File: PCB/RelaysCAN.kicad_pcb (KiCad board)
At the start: 2 copper layers, 200 x 100 mm, 99 parts, among them J1 Screw_Terminal_01x03, J2 Screw_Terminal_01x02, J3 Conn_01x24_Male, J4 Conn_01x24_Male, J5 Conn_01x24_Male, J6 Conn_01x24_Male, J7 Conn_01x24_Male, J8 Conn_01x24_Male, K1 ALQ112, K10 ALQ112, K11 ALQ112, K12 ALQ112, K13 ALQ112, K14 ALQ112, K15 ALQ112, K16 ALQ112, K17 ALQ112, K18 ALQ112, K19 ALQ112, K2 ALQ112, K20 ALQ112, K21 ALQ112, K22 ALQ112, K23 ALQ112, K24 ALQ112, K3 ALQ112, K4 ALQ112, K5 ALQ112, K6 ALQ112, K7 ALQ112, K8 ALQ112, K9 ALQ112, U1 MCP2562-E-P, U2 MCP2515-IP, U3 ATmega88A-PU, U4 MCP23017_SP, U5 ULN2803A, U6 ULN2803A, U7 ULN2803A

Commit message: Update PCB.
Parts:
- added C6: 22pF, Capacitor_THT:C_Disc_D4.3mm_W1.9mm_P5.00mm, F.Cu at (233.6, 57.0)
- added C7: 22pF, Capacitor_THT:C_Disc_D4.3mm_W1.9mm_P5.00mm, F.Cu at (219.2, 57.1)
- added JP2: SolderJumper_2_Bridged, Jumper:SolderJumper-2_P1.3mm_Open_RoundedPad1.0x1.5mm, B.Cu at (210.7, 54.1)
- added Y1: 16MHz, Crystal:Crystal_HC18-U_Vertical, F.Cu at (228.9, 58.9)
- moved R1 9.26 mm to (226.2, 66.8), turned to 180 degrees
- moved JP1 4.93 mm to (231.4, 65.0), turned to 0 degrees
- moved J1 3.19 mm to (239.4, 68.6)
- moved U1 1.78 mm to (207.8, 58.4)
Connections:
- U2 pad 3: Net-(U2-Pad3) -> /CLKOUT
- U2 pad 8: /CLKO -> Net-(C6-Pad1)
- U3 pad 9: Net-(U3-Pad9) -> /CLKOUT
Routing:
- net Net-(C6-Pad1): track 0.00 -> 38.3 mm, vias 0 -> 2
- net /CLKOUT: track 0.00 -> 29.3 mm
- net /CLKO: track 26.3 -> 2.70 mm
- net Net-(C7-Pad1): track 0.00 -> 14.4 mm
- net GND: track 301.4 -> 312.3 mm
- net /CANH: track 20.0 -> 27.0 mm
- net /CANL: track 21.0 -> 27.2 mm
- net +5V: track 380.3 -> 376.8 mm
- net /TXCAN: track 7.18 -> 9.71 mm
- net /RXCAN: track 18.2 -> 19.6 mm
- net /SCK: track 36.6 -> 37.8 mm
- net Net-(JP1-Pad2): track 6.35 -> 5.52 mm
- net /INT: track 49.7 -> 48.9 mm
- net /MOSI: track 28.1 -> 28.6 mm

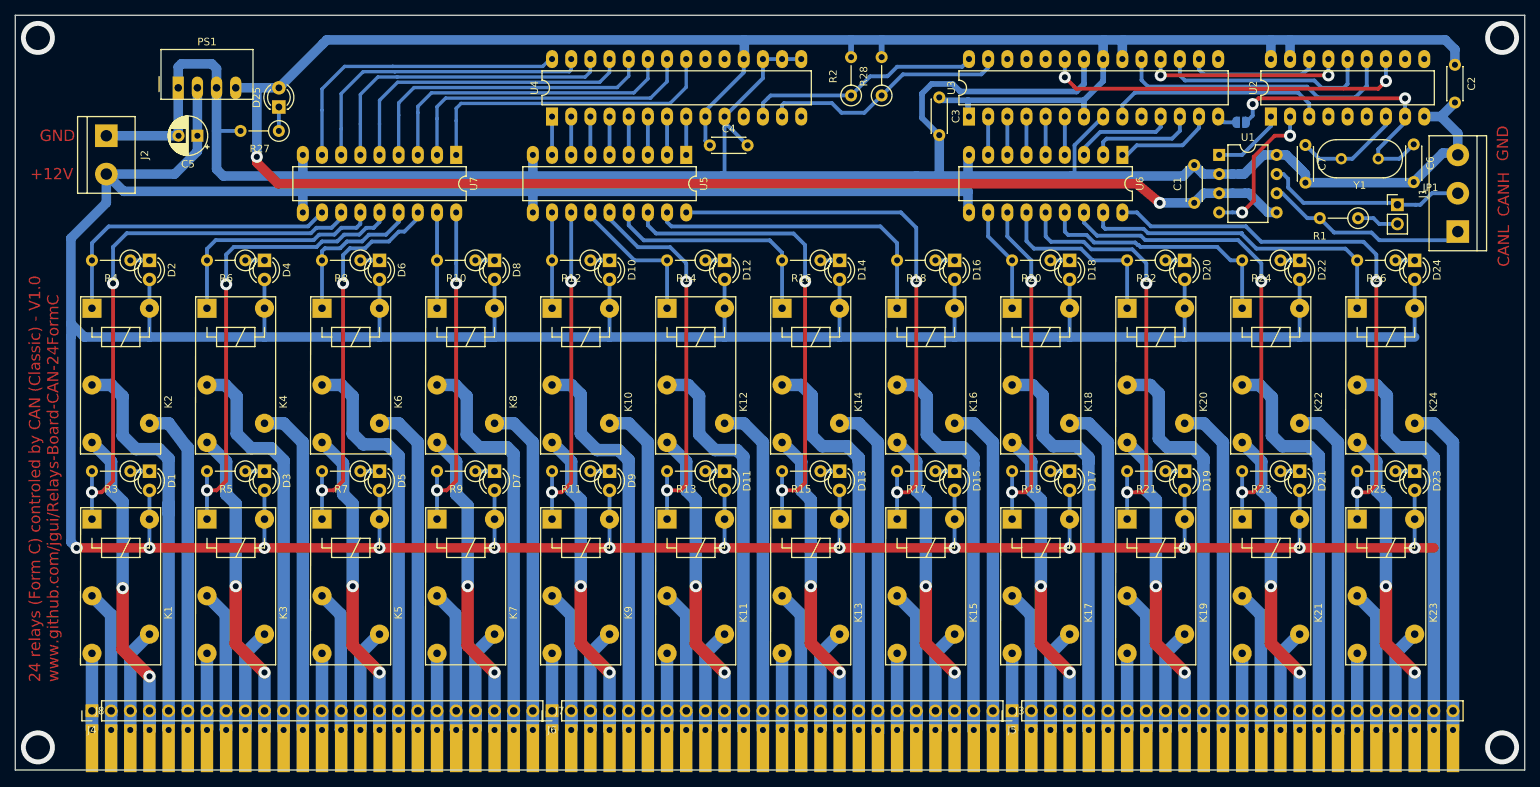
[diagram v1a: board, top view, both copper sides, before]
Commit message: Add a jumper to enter configuration mode.
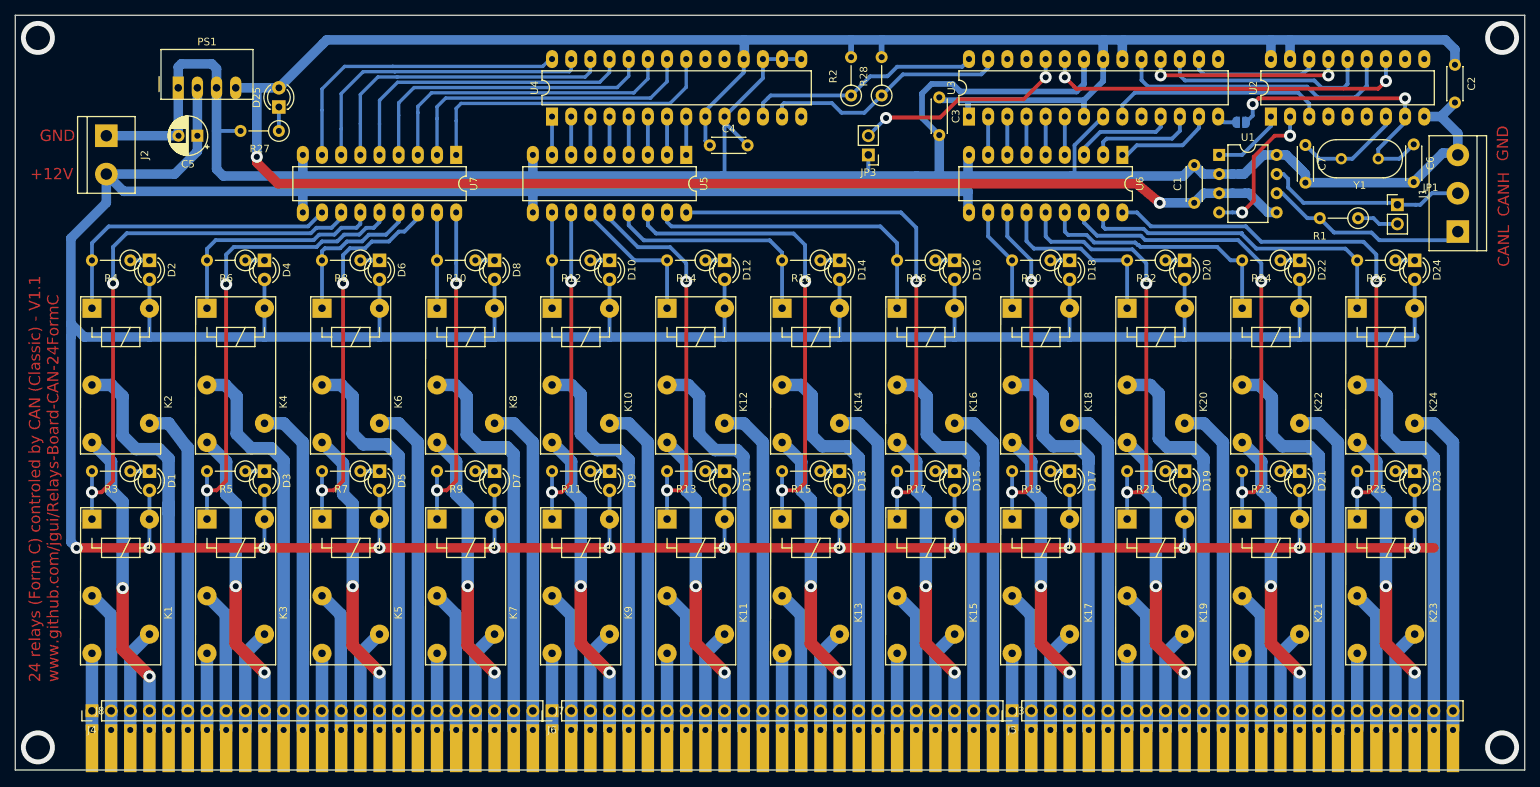
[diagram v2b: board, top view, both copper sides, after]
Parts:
- added JP3: Jumper, Connector_PinHeader_2.54mm:PinHeader_1x02_P2.54mm_Vertical, F.Cu at (161.3, 58.4)
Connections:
- U3 pad 24: Net-(U3-Pad24) -> /CONF
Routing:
- net /CONF: track 0.00 -> 29.1 mm, vias 0 -> 2
- net GND: track 312.3 -> 315.1 mm
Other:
- board text added: "24 relays (Form C) controled by CAN (Classic) - V1.1 www.github.com/jgui/Relays-Board-CAN-24FormC"
- board text removed: "24 relays (Form C) controled by CAN (Classic) - V1.0 www.github.com/jgui/Relays-Board-CAN-24FormC"
